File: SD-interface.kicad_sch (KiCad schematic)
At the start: 18 parts, among them J8 SD_Card_Receptacle, U15 GL3224-OIY04, U16 TPD4E02B04DQA, U17 TPD4E02B04DQA, Y2 25MHz +-0.03%

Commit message: Added lcsc part number for most of components, fixes for better routing
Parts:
- C70, C71, C72, C73, C76, C77: LCSC Part (none) -> C5182432
- C74, C75: LCSC Part (none) -> C18164591
- C78, C79: value C -> 18pF; LCSC Part (none) -> C33149
- D5: footprint Diode_SMD:D_0603_1608Metric -> LED_SMD:LED_0603_1608Metric; LCSC Part (none) -> C22371298
- U16, U17: LCSC Part (none) -> C106794
- Y2: footprint Crystal:Crystal_SMD_0603-4Pin_6.0x3.5mm -> Crystal:Crystal_SMD_3225-4Pin_3.2x2.5mm; LCSC Part (none) -> C179643
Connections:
- net GND: now also Y2.4; no longer Y2.3
- net SD_CD: now also U16.1 (IO1), U16.10 (NC); no longer U17.4 (IO3), U17.7 (NC)
- net SD_CK: now also U17.5 (IO4), U17.6 (NC); no longer U17.1 (IO1), U17.10 (NC)
- net SD_CM: now also U16.2 (IO2), U16.9 (NC); no longer U17.2 (IO2), U17.9 (NC)
- net SD_D0: now also U17.4 (IO3), U17.7 (NC); no longer U16.1 (IO1), U16.10 (NC)
- net SD_D1: now also U17.2 (IO2), U17.9 (NC); no longer U16.2 (IO2), U16.9 (NC)
- net SD_D2: now also U16.5 (IO4), U16.6 (NC); no longer U16.4 (IO3), U16.7 (NC)
- net SD_D3: now also U16.4 (IO3), U16.7 (NC); no longer U16.5 (IO4), U16.6 (NC)
- net SD_WP: now also U17.1 (IO1), U17.10 (NC); no longer U17.5 (IO4), U17.6 (NC)
- net XOUT: now also Y2.3; no longer Y2.4

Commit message: Added lcsc part number for most of resistors
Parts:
- R58: LCSC Part (none) -> C25130
- R59: value 520 -> 560; LCSC Part (none) -> C137858
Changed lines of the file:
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@@
+			)
+		)
+		(property "LCSC Part" "C25130"
+			(at 121.92 106.68 90)
+			(effects
+				(font
+					(size 1.27 1.27)
+				)
+				(hide yes)
 			)
 		)
@@
 			)
 		)
-		(property "Value" "520"
+		(property "Value" "560"
 			(at 74.93 107.95 90)
 			(effects
@@
 			(effects
 				(font
+					(size 1.27 1.27)
+				)
+				(hide yes)
+			)
+		)
+		(property "LCSC Part" "C137858 "
+			(at 74.93 111.76 90)
+			(effects
+				(font

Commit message: comments to schematic added, changed a few components
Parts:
- J8: footprint Connector_Card:SD_Kyocera_145638009511859+ -> SamacSys_Parts:SD2A; Mouser Part No  (none) -> 179-SD-2-A
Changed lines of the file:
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@@
 			)
 		)
-		(property "Footprint" "Connector_Card:SD_Kyocera_145638009511859+"
+		(property "Footprint" "SamacSys_Parts:SD2A"
 			(at 256.54 52.832 0)
 			(effects
@@
 			(at 247.65 49.53 0)
 			(effects
+				(font
+					(size 1.27 1.27)
+				)
+				(hide yes)
+			)
+		)
+		(property "Mouser Part No " "179-SD-2-A "
+			(at 247.65 49.53 0)
+			(effects

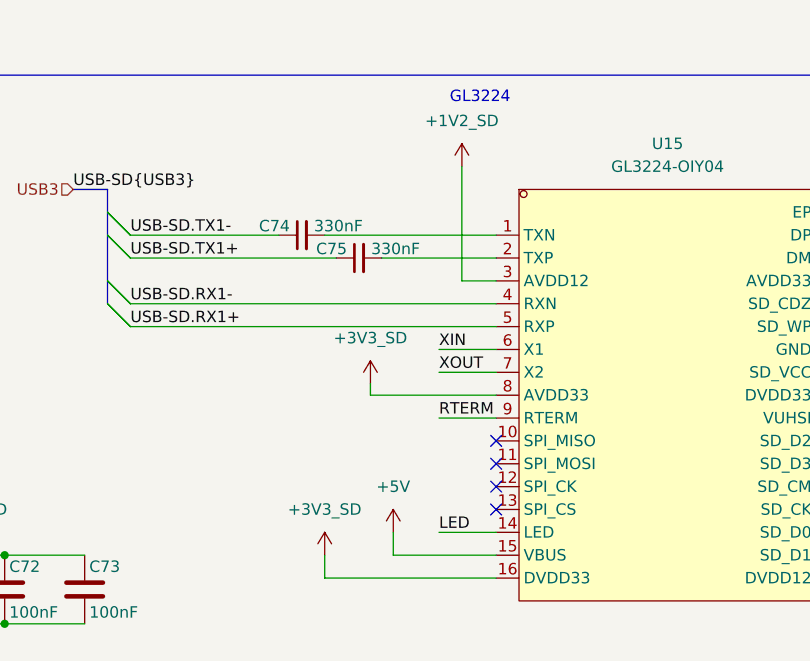
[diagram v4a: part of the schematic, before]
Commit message: Rearrange of the component placement, scheme changes for better routing
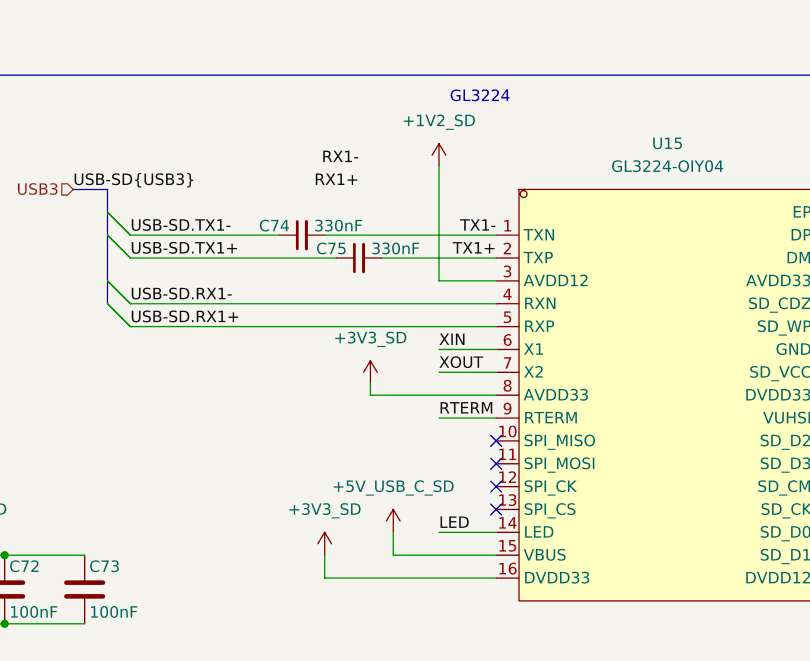
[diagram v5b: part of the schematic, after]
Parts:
- C70, C71, C72, C73, C76, C77: footprint Capacitor_SMD:C_0402_1005Metric -> Capacitor_SMD:C_0201_0603Metric; LCSC Part C5182432 -> C181043
- C74, C75: footprint Capacitor_SMD:C_0402_1005Metric -> Capacitor_SMD:C_0201_0603Metric; LCSC Part C18164591 -> C2980695
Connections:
- net TX1+: now reaches C75.2, U15.2 (TXP)
- net TX1-: now reaches C74.2, U15.1 (TXN)
- net +5V renamed +5V_USB_C_SD
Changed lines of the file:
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@@
 	(wire
 		(pts
-			(xy 90.17 30.48) (xy 90.17 43.18)
+			(xy 87.63 30.48) (xy 87.63 43.18)
 		)
 		(stroke
@@
 	(wire
 		(pts
-			(xy 90.17 43.18) (xy 93.98 43.18)
+			(xy 87.63 43.18) (xy 93.98 43.18)
 		)
 		(stroke
@@
 		)
 	)
+	(label "RX1-"
+		(at 78.74 30.48 180)
+		(effects
+			(font
+				(size 1.27 1.27)
+			)
+			(justify right bottom)
+		)
+	)
 	(label "XOUT"
 		(at 87.63 53.34 0)
@@
 		)
 	)
+	(label "TX1-"
+		(at 93.98 38.1 180)
+		(effects
+			(font
+				(size 1.27 1.27)
+			)
+			(justify right bottom)
+		)
+	)
 	(label "SD_CD"
 		(at 267.97 39.37 0)
@@
 		)
 	)
+	(label "RX1+"
+		(at 78.74 33.02 180)
+		(effects
+			(font
+				(size 1.27 1.27)
+			)
+			(justify right bottom)
+		)
+	)
 	(label "RTERM"
 		(at 87.63 58.42 0)
@@
 		)
 	)
+	(label "TX1+"
+		(at 93.98 40.64 180)
+		(effects
+			(font
+				(size 1.27 1.27)
+			)
+			(justify right bottom)
+		)
+	)
 	(hierarchical_label "USB3"
 		(shape input)
@@
 			)
 		)
-		(property "Footprint" "Capacitor_SMD:C_0402_1005Metric"
+		(property "Footprint" "Capacitor_SMD:C_0201_0603Metric"
 			(at 21.2852 60.96 0)
 			(effects
@@
 			)
 		)
-		(property "LCSC Part" "C5182432"
+		(property "LCSC Part" "C181043 "
 			(at 20.32 57.15 0)
 			(effects
@@
 			)
 		)
-		(property "Footprint" "Capacitor_SMD:C_0402_1005Metric"
+		(property "Footprint" "Capacitor_SMD:C_0201_0603Metric"
 			(at 49.2252 81.28 0)
 			(effects
@@
 			)
 		)
-		(property "LCSC Part" "C5182432"
+		(property "LCSC Part" "C181043 "
 			(at 48.26 77.47 0)
 			(effects
@@
 			)
 		)
-		(property "Footprint" "Capacitor_SMD:C_0402_1005Metric"
+		(property "Footprint" "Capacitor_SMD:C_0201_0603Metric"
 			(at 78.74 40.64 0)
 			(effects
@@
 			)
 		)
-		(property "LCSC Part" "C18164591"
+		(property "LCSC Part" "C2980695 "
 			(at 78.74 40.64 90)
 			(effects
@@
 			)
 		)
-		(property "Footprint" "Capacitor_SMD:C_0402_1005Metric"
+		(property "Footprint" "Capacitor_SMD:C_0201_0603Metric"
 			(at 31.4452 81.28 0)
 			(effects
@@
 			)
 		)
-		(property "LCSC Part" "C5182432"
+		(property "LCSC Part" "C181043 "
 			(at 30.48 77.47 0)
 			(effects
@@
 	)
 	(symbol
-		(lib_id "power:+5V")
-		(at 82.55 71.12 0)
-		(unit 1)
-		(exclude_from_sim no)
-		(in_bom yes)
-		(on_board yes)
-		(dnp no)
-		(fields_autoplaced yes)
-		(property "Reference" "#PWR0123"
-			(at 82.55 74.93 0)
-			(effects
-				(font
-					(size 1.27 1.27)
-				)
-				(hide yes)
-			)
-		)
-		(property "Value" "+5V"
-			(at 82.55 66.04 0)
-			(effects
-				(font
-					(size 1.27 1.27)
-				)
-			)
-		)
-		(property "Footprint" ""
-			(at 82.55 71.12 0)
-			(effects
-				(font
-					(size 1.27 1.27)
-				)
-				(hide yes)
-			)
-		)
-		(property "Datasheet" ""
-			(at 82.55 71.12 0)
-			(effects
-				(font
-					(size 1.27 1.27)
-				)
-				(hide yes)
-			)
-		)
-		(property "Description" "Power symbol creates a global label with name \"+5V\""
-			(at 82.55 71.12 0)
-			(effects
-				(font
-					(size 1.27 1.27)
-				)
-				(hide yes)
-			)
-		)
-		(pin "1"
-		)
-		(instances
-			(project ""
-				(path "/a2586c28-95f1-49e6-9254-37d7a8473e53/9b23769b-d955-4774-b8ac-278fd96aa141"
-					(reference "#PWR0123")
-					(unit 1)
-				)
-			)
-		)
-	)
-	(symbol
 		(lib_id "power:+1V1")
 		(at 247.65 29.21 0)
@@
 			)
 		)
-		(property "Footprint" "Capacitor_SMD:C_0402_1005Metric"
+		(property "Footprint" "Capacitor_SMD:C_0201_0603Metric"
 			(at 72.39 38.1 0)
 			(effects
@@
 			)
 		)
-		(property "LCSC Part" "C18164591"
+		(property "LCSC Part" "C2980695 "
 			(at 72.39 38.1 90)
 			(effects
@@
 			)
 		)
-		(property "Footprint" "Capacitor_SMD:C_0402_1005Metric"
+		(property "Footprint" "Capacitor_SMD:C_0201_0603Metric"
 			(at 40.3352 81.28 0)
 			(effects
@@
 			)
 		)
-		(property "LCSC Part" "C5182432"
+		(property "LCSC Part" "C181043 "
 			(at 39.37 77.47 0)
 			(effects
@@
 		(on_board yes)
 		(dnp no)
-		(fields_autoplaced yes)
 		(property "Reference" "U15"
 			(at 113.03 27.94 0)
@@
 			)
 		)
-		(property "Footprint" "Capacitor_SMD:C_0402_1005Metric"
+		(property "Footprint" "Capacitor_SMD:C_0201_0603Metric"
 			(at 30.1752 60.96 0)
 			(effects
@@
 			)
 		)
-		(property "LCSC Part" "C5182432"
+		(property "LCSC Part" "C181043 "
 			(at 29.21 57.15 0)
 			(effects
@@
 			)
 		)
-		(property "Footprint" "Capacitor_SMD:C_0402_1005Metric"
+		(property "Footprint" "Capacitor_SMD:C_0201_0603Metric"
 			(at 21.2852 81.28 0)
 			(effects
@@
 			)
 		)
-		(property "LCSC Part" "C5182432"
+		(property "LCSC Part" "C181043 "
 			(at 20.32 77.47 0)
 			(effects
@@
 	(symbol
 		(lib_id "power:+1V2")
-		(at 90.17 30.48 0)
+		(at 87.63 30.48 0)
 		(unit 1)
 		(exclude_from_sim no)
@@
 		(fields_autoplaced yes)
 		(property "Reference" "#PWR0115"
-			(at 90.17 34.29 0)
+			(at 87.63 34.29 0)
 			(effects
 				(font
@@
 		)
 		(property "Value" "+1V2_SD"
-			(at 90.17 25.4 0)
+			(at 87.63 25.4 0)
 			(effects
 				(font
@@
 		)
 		(property "Footprint" ""
-			(at 90.17 30.48 0)
+			(at 87.63 30.48 0)
 			(effects
 				(font
@@
 		)
 		(property "Datasheet" ""
-			(at 90.17 30.48 0)
+			(at 87.63 30.48 0)
 			(effects
 				(font
@@
 		)
 		(property "Description" "Power symbol creates a global label with name \"+1V2\""
-			(at 90.17 30.48 0)
+			(at 87.63 30.48 0)
 			(effects
 				(font
@@
 					(unit 1)
 				)
+			)
+		)
+	)
+	(symbol
+		(lib_id "power:+5V")
+		(at 82.55 71.12 0)
+		(unit 1)
+		(exclude_from_sim no)
+		(in_bom yes)
+		(on_board yes)
+		(dnp no)
+		(fields_autoplaced yes)
+		(property "Reference" "#PWR0123"
+			(at 82.55 74.93 0)
+			(effects
+				(font
+					(size 1.27 1.27)
+				)
+				(hide yes)
+			)
+		)
+		(property "Value" "+5V_USB_C_SD"
+			(at 82.55 66.04 0)
+			(effects
+				(font
+					(size 1.27 1.27)
+				)
+			)
+		)
+		(property "Footprint" ""
+			(at 82.55 71.12 0)
+			(effects
+				(font
+					(size 1.27 1.27)
+				)
+				(hide yes)
+			)
+		)
+		(property "Datasheet" ""
+			(at 82.55 71.12 0)
+			(effects
+				(font
+					(size 1.27 1.27)
+				)
+				(hide yes)
+			)
+		)
+		(property "Description" "Power symbol creates a global label with name \"+5V\""
+			(at 82.55 71.12 0)
+			(effects
+				(font
+					(size 1.27 1.27)
+				)
+				(hide yes)
+			)
+		)
+		(pin "1"
+		)
+		(instances
+			(project "USB_hub"
+				(path "/a2586c28-95f1-49e6-9254-37d7a8473e53/9b23769b-d955-4774-b8ac-278fd96aa141"
+					(reference "#PWR0123")
+					(unit 1)
+				)
